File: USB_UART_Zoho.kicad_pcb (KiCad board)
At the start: 2 copper layers, 48.7 x 23.6 mm, 24 parts, among them J1 USB_C_Receptacle, J2 Peripherals, J3 Cbus, J4 VccIo_jumper, J5 POWER, U1 FT232RL, U2 USBLC6-2P6

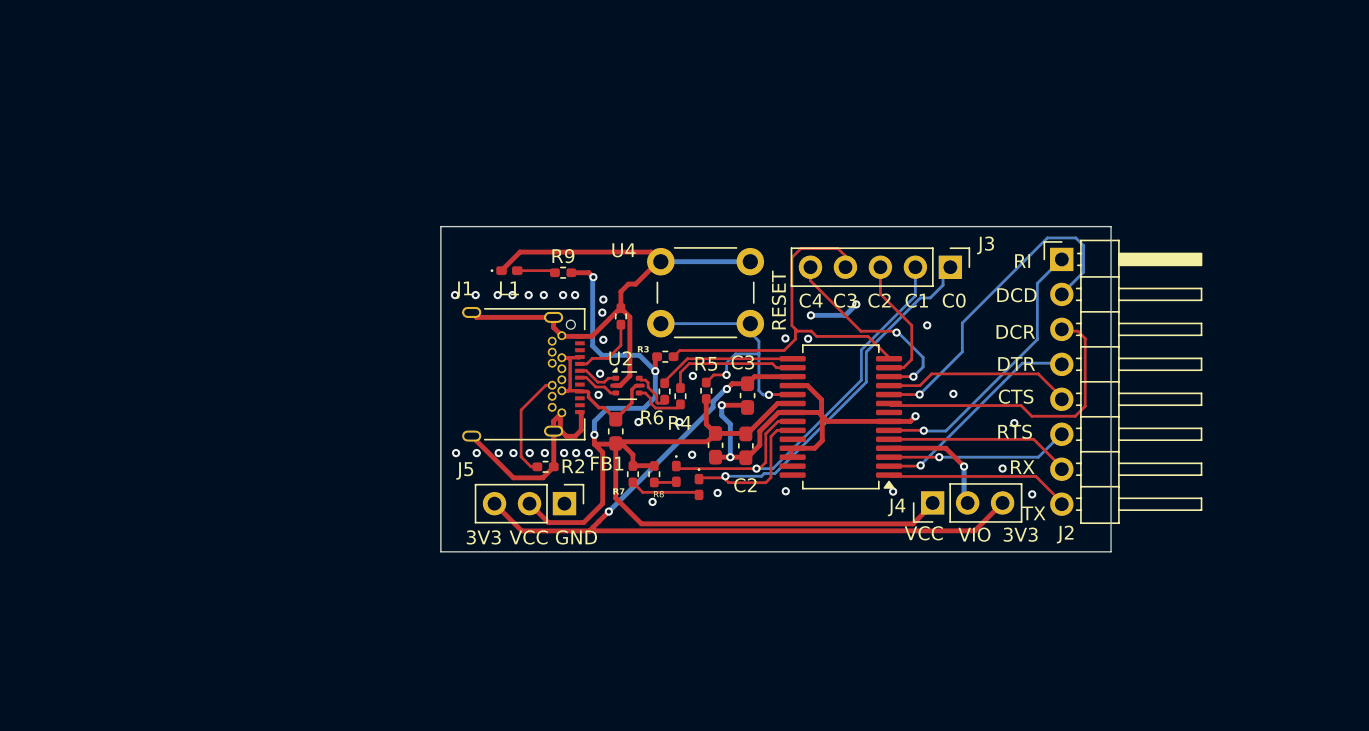
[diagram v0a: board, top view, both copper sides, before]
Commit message: improved design decisions from the previous layout
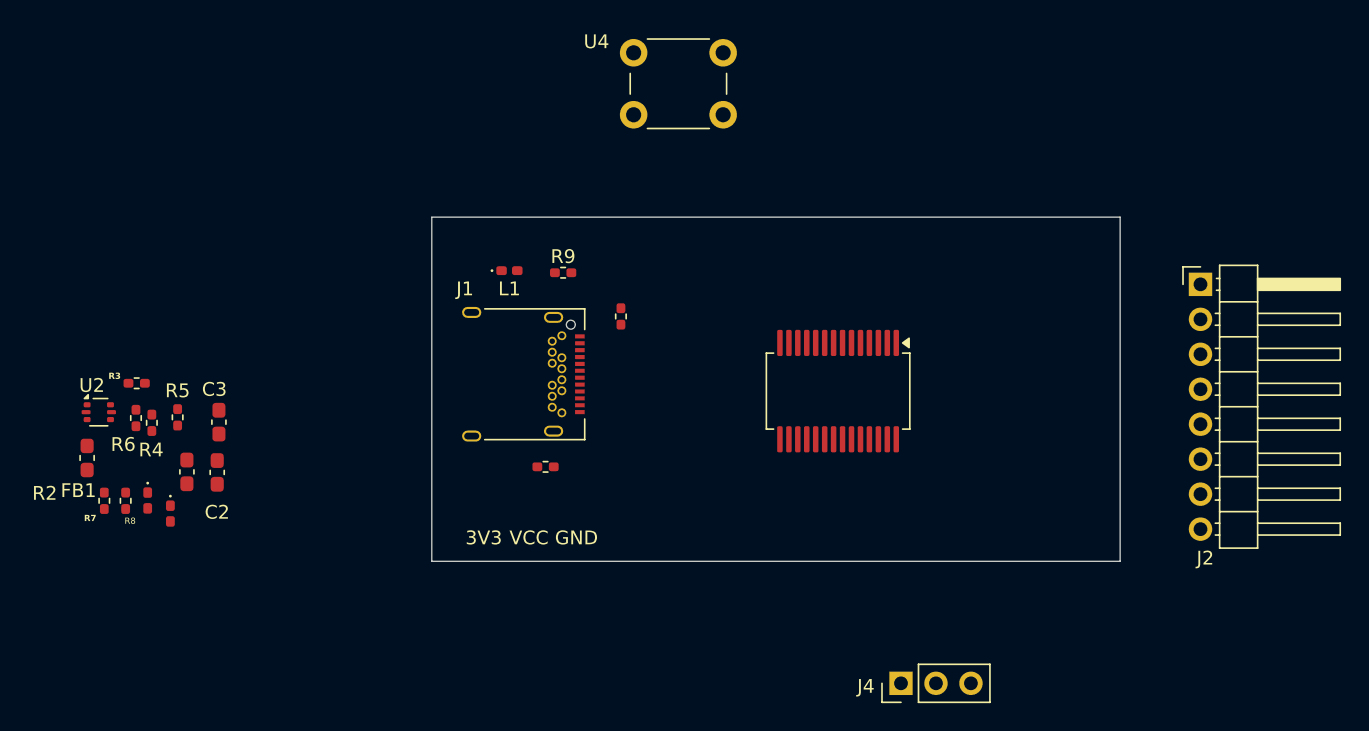
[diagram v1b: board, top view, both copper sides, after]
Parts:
- removed J3: Cbus, Connector_PinHeader_2.54mm:PinHeader_1x05_P2.54mm_Vertical
- removed J5: POWER, Connector_PinHeader_2.54mm:PinHeader_1x03_P2.54mm_Vertical
- moved C1 38.4 mm to (109.5, 102.1)
- moved FB1 38.4 mm to (102.2, 101.1)
- moved R6 38.4 mm to (105.8, 98.2)
- moved R7 38.4 mm to (103.5, 104.2)
- moved R8 38.4 mm to (105.0, 104.2)
- moved Rx_LED1 38.4 mm to (106.6, 104.2)
- moved Tx_LED1 38.4 mm to (108.3, 105.1)
- moved C2 38.4 mm to (111.7, 102.2)
- moved C3 38.4 mm to (111.8, 98.5)
- moved R3 38.4 mm to (105.8, 95.7)
- moved R4 38.4 mm to (106.9, 98.6)
- moved R5 38.4 mm to (108.8, 98.2)
- moved U2 38.4 mm to (103.1, 97.8)
- moved U4 15.3 mm to (148.4, 76.2)
- moved J4 13.3 mm to (161.3, 117.5)
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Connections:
- net /CBUS0 renamed Net-(Tx_LED1-K)
- net /CBUS1 renamed Net-(Rx_LED1-K)
- net /CBUS3 renamed Net-(U1-CBUS3)
- J1 pad A6: /D1+ -> /D+
- J1 pad A7: /D1- -> /D-
- J1 pad B6: unconnected-(J1-D+-PadB6) -> /D+
- J1 pad B7: unconnected-(J1-D--PadB7) -> /D-
- J2 pad 1: /RI -> unconnected-(J2-Pin_1-Pad1)
- J2 pad 2: /DCD -> unconnected-(J2-Pin_2-Pad2)
- J2 pad 3: /DCR -> unconnected-(J2-Pin_3-Pad3)
- J2 pad 4: /DTR -> unconnected-(J2-Pin_4-Pad4)
- J2 pad 5: /CTS -> unconnected-(J2-Pin_5-Pad5)
- J2 pad 6: /RTS -> unconnected-(J2-Pin_6-Pad6)
- J2 pad 7: /Rx -> unconnected-(J2-Pin_7-Pad7)
- J2 pad 8: /Tx -> unconnected-(J2-Pin_8-Pad8)
- R4 pad 1: /D1- -> /D-
- R4 pad 2: D- -> /d_N
- R6 pad 1: /D1+ -> /D+
- R6 pad 2: D+ -> /d_P
- U1 pad 1: /Tx -> unconnected-(U1-TXD-Pad1)
- U1 pad 10: /DCD -> unconnected-(U1-DCD-Pad10)
- U1 pad 11: /CTS -> unconnected-(U1-CTS-Pad11)
- U1 pad 12: /CBUS4 -> unconnected-(U1-CBUS4-Pad12)
- U1 pad 13: /CBUS2 -> unconnected-(U1-CBUS2-Pad13)
- U1 pad 15: D+ -> /d+
- U1 pad 16: D- -> /d-
- U1 pad 2: /DTR -> unconnected-(U1-DTR-Pad2)
- U1 pad 3: /RTS -> unconnected-(U1-RTS-Pad3)
- U1 pad 5: /Rx -> unconnected-(U1-RXD-Pad5)
- U1 pad 6: /RI -> unconnected-(U1-RI-Pad6)
- U1 pad 9: /DCR -> unconnected-(U1-DCR-Pad9)
- U2 pad 1: /D1+ -> /d_N
- U2 pad 3: /D1- -> /d_P
- U2 pad 4: /D1- -> /d+
- U2 pad 6: /D1+ -> /d-
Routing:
- net GND: track 94.8 -> 0.00 mm, vias 42 -> 0
- net VCC: track 84.7 -> 0.00 mm, vias 3 -> 0
- net 3V3OUT: track 58.1 -> 0.00 mm, vias 2 -> 0
- net Net-(Tx_LED1-K): track 34.9 -> 0.00 mm, vias 1 -> 0
- net Net-(Rx_LED1-K): track 31.2 -> 0.00 mm, vias 1 -> 0
- net Net-(U1-CBUS3): track 28.4 -> 0.00 mm
- net /DCD: track 24.3 -> 0.00 mm, vias 1 -> 0
- net /DCR: track 21.8 -> 0.00 mm
- net /RI: track 20.1 -> 0.00 mm, vias 1 -> 0
- net /RESET: track 20.0 -> 0.00 mm, vias 2 -> 0
- net /DTR: track 15.6 -> 0.00 mm, vias 1 -> 0
- net /CBUS4: track 14.8 -> 0.00 mm, vias 2 -> 0
- net /CTS: track 13.6 -> 0.00 mm
- net /Rx: track 13.4 -> 0.00 mm
- net /Tx: track 13.3 -> 0.00 mm
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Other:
- board size 48.7 x 23.6 mm -> 50 x 25 mm
- copper layers 2 -> 4
- board text removed: "C0"
- board text removed: "C1"
- board text removed: "C2"
- board text removed: "C3"
- board text removed: "C4"
- board text removed: "CTS"
- board text removed: "DCD"
- board text removed: "DCR"
- board text removed: "DTR"
- board text removed: "RESET"
- board text removed: "RI"
- board text removed: "RTS"
- board text removed: "RX"
- board text removed: "TX"
- board text removed: "VIO"
